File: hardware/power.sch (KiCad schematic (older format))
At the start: 34 parts, among them U1 TPS54526_PWP, U2 LT1761_1, U3 MIC2774N

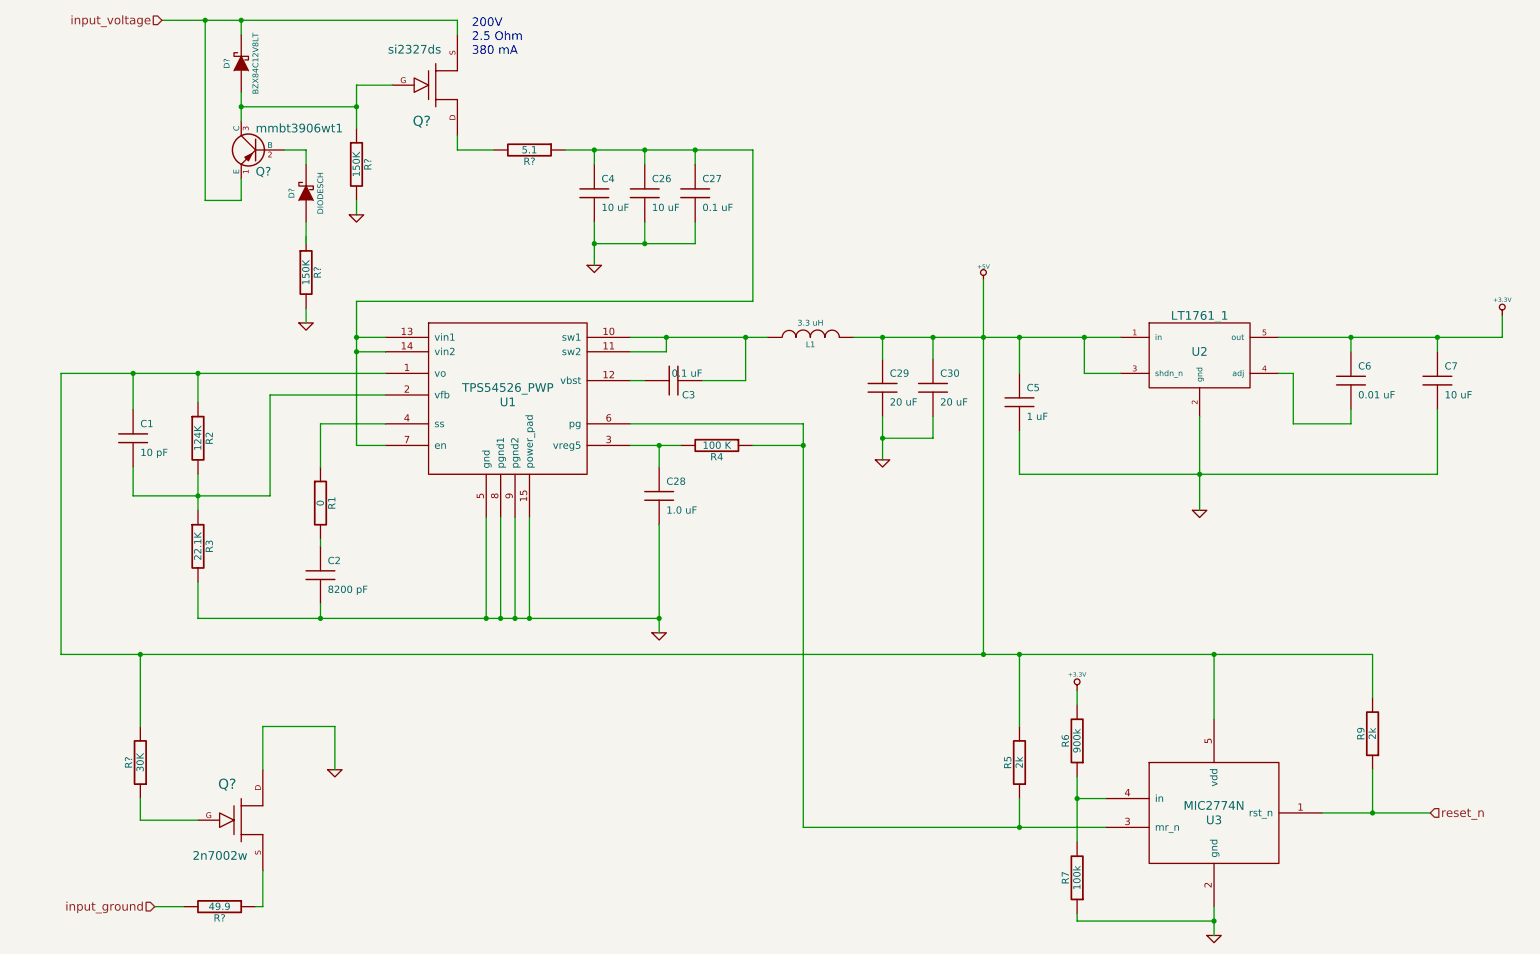
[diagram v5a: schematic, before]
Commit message: added RCT and accellerometer, added new sheet
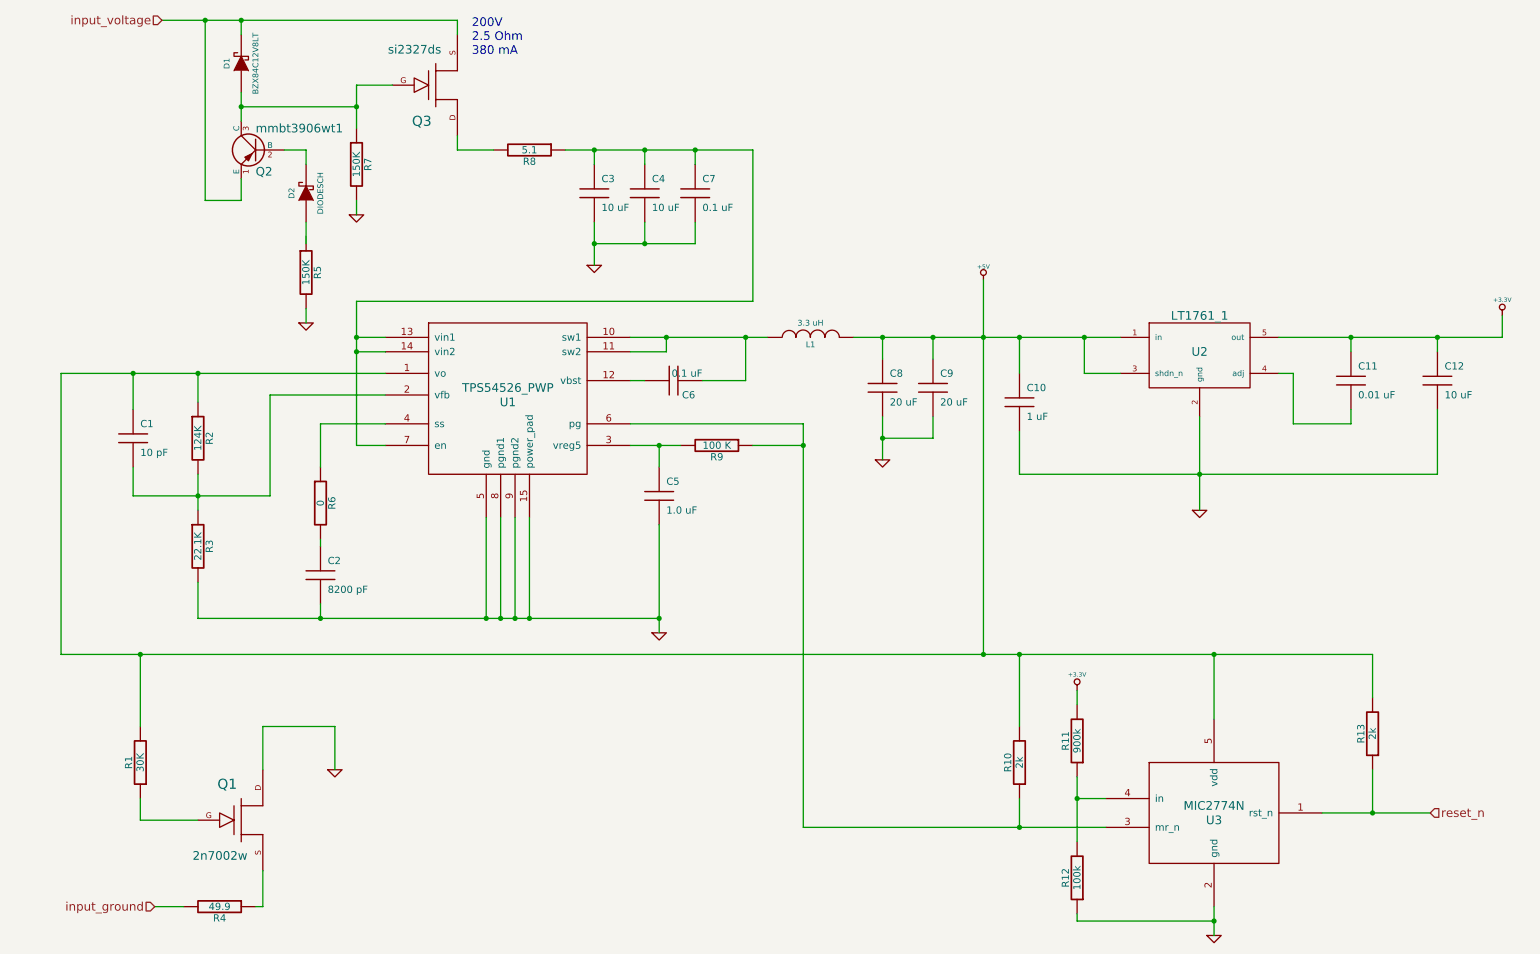
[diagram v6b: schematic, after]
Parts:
- gave numbers to parts that had none: 10
- renumbered C5 to C10, C6 to C11, C7 to C12, C4 to C3, C26 to C4, C28 to C5, C3 to C6, C27 to C7, C29 to C8, C30 to C9, R5 to R10, R6 to R11, R7 to R12, R9 to R13, R1 to R6, R4 to R9
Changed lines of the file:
@@
-EESchema Schematic File Version 2  date Thu 07 Nov 2013 07:55:20 AM EST
+EESchema Schematic File Version 2  date Tue 12 Nov 2013 10:09:33 PM EST
 LIBS:power
 LIBS:device
@@
 $Descr A4 11700 8267
 encoding utf-8
-Sheet 2 5
+Sheet 2 6
 Title ""
-Date "7 nov 2013"
+Date "13 nov 2013"
 Rev ""
 Comp ""
@@
 Connection ~ 4550 1600
 $Comp
-L R R?
+L R R8
 U 1 1 527B8B5E
 P 4100 1600
-F 0 "R?" V 4180 1600 50  0000 C CNN
+F 0 "R8" V 4180 1600 50  0000 C CNN
 F 1 "5.1" V 4100 1600 50  0000 C CNN
 	1    4100 1600
@@
 200V \n2.5 Ohm \n380 mA
 $Comp
-L FET_N Q?
+L FET_N Q3
 U 1 1 527B8896
 P 3450 1150
-F 0 "Q?" H 3353 1400 70  0000 C CNN
+F 0 "Q3" H 3353 1400 70  0000 C CNN
 F 1 "si2327ds" H 3303 903 60  0000 C CNN
 	1    3450 1150
@@
 $EndComp
 $Comp
-L R R?
+L R R7
 U 1 1 527B886A
 P 2900 1700
-F 0 "R?" V 2980 1700 50  0000 C CNN
+F 0 "R7" V 2980 1700 50  0000 C CNN
 F 1 "150K" V 2900 1700 50  0000 C CNN
 	1    2900 1700
@@
 $EndComp
 $Comp
-L GND #PWR?
+L GND #PWR01
 U 1 1 527B8869
 P 2900 2050
-F 0 "#PWR?" H 2900 2050 30  0001 C CNN
+F 0 "#PWR01" H 2900 2050 30  0001 C CNN
 F 1 "GND" H 2900 1980 30  0001 C CNN
 	1    2900 2050
@@
 $EndComp
 $Comp
-L DIODESCH D?
+L DIODESCH D1
 U 1 1 527B8850
 P 2100 1000
-F 0 "D?" H 2100 1100 40  0000 C CNN
+F 0 "D1" H 2100 1100 40  0000 C CNN
 F 1 "BZX84C12V8LT" H 2100 900 40  0000 C CNN
 	1    2100 1000
@@
 $EndComp
 $Comp
-L GND #PWR?
+L GND #PWR02
 U 1 1 527B883D
 P 2550 2800
-F 0 "#PWR?" H 2550 2800 30  0001 C CNN
+F 0 "#PWR02" H 2550 2800 30  0001 C CNN
 F 1 "GND" H 2550 2730 30  0001 C CNN
 	1    2550 2800
@@
 $EndComp
 $Comp
-L R R?
+L R R5
 U 1 1 527B882C
 P 2550 2450
-F 0 "R?" V 2630 2450 50  0000 C CNN
+F 0 "R5" V 2630 2450 50  0000 C CNN
 F 1 "150K" V 2550 2450 50  0000 C CNN
 	1    2550 2450
@@
 $EndComp
 $Comp
-L R R?
+L R R4
 U 1 1 527B85F0
 P 1950 6850
-F 0 "R?" V 2030 6850 50  0000 C CNN
+F 0 "R4" V 2030 6850 50  0000 C CNN
 F 1 "49.9" V 1950 6850 50  0000 C CNN
 	1    1950 6850
@@
 $EndComp
 $Comp
-L GND #PWR?
+L GND #PWR03
 U 1 1 527B85B8
 P 2750 5900
-F 0 "#PWR?" H 2750 5900 30  0001 C CNN
+F 0 "#PWR03" H 2750 5900 30  0001 C CNN
 F 1 "GND" H 2750 5830 30  0001 C CNN
 	1    2750 5900
@@
 $EndComp
 $Comp
-L R R?
+L R R1
 U 1 1 527B8568
 P 1400 5850
-F 0 "R?" V 1480 5850 50  0000 C CNN
+F 0 "R1" V 1480 5850 50  0000 C CNN
 F 1 "30K" V 1400 5850 50  0000 C CNN
 	1    1400 5850
@@
 $EndComp
 $Comp
-L FET_N Q?
+L FET_N Q1
 U 1 1 527B8523
 P 2100 6250
-F 0 "Q?" H 2003 6500 70  0000 C CNN
+F 0 "Q1" H 2003 6500 70  0000 C CNN
 F 1 "2n7002w" H 1953 6003 60  0000 C CNN
 	1    2100 6250
@@
 $EndComp
 $Comp
-L PNP Q?
+L PNP Q2
 U 1 1 527B8379
 P 2200 1600
-F 0 "Q?" H 2200 1450 60  0000 R CNN
+F 0 "Q2" H 2200 1450 60  0000 R CNN
 F 1 "mmbt3906wt1" H 2200 1750 60  0000 R CNN
 	1    2200 1600
@@
 $EndComp
 $Comp
-L DIODESCH D?
+L DIODESCH D2
 U 1 1 527B82DF
 P 2550 1900
-F 0 "D?" H 2550 2000 40  0000 C CNN
+F 0 "D2" H 2550 2000 40  0000 C CNN
 F 1 "DIODESCH" H 2550 1800 40  0000 C CNN
 	1    2550 1900
@@
 $EndComp
 $Comp
-L C C28
+L C C5
 U 1 1 5278578C
 P 5000 4000
-F 0 "C28" H 5050 4100 50  0000 L CNN
+F 0 "C5" H 5050 4100 50  0000 L CNN
 F 1 "1.0 uF" H 5050 3900 50  0000 L CNN
 	1    5000 4000
@@
 $EndComp
 $Comp
-L R R4
+L R R9
 U 1 1 52785766
 P 5400 3650
-F 0 "R4" V 5480 3650 50  0000 C CNN
+F 0 "R9" V 5480 3650 50  0000 C CNN
 F 1 "100 K" V 5400 3650 50  0000 C CNN
 	1    5400 3650
@@
 $EndComp
 $Comp
-L C C29
+L C C8
 U 1 1 527852FE
 P 6550 3250
-F 0 "C29" H 6600 3350 50  0000 L CNN
+F 0 "C8" H 6600 3350 50  0000 L CNN
 F 1 "20 uF" H 6600 3150 50  0000 L CNN
 	1    6550 3250
@@
 $EndComp
 $Comp
-L C C30
+L C C9
 U 1 1 527852FD
 P 6900 3250
-F 0 "C30" H 6950 3350 50  0000 L CNN
+F 0 "C9" H 6950 3350 50  0000 L CNN
 F 1 "20 uF" H 6950 3150 50  0000 L CNN
 	1    6900 3250
@@
 $EndComp
 $Comp
-L GND #PWR01
+L GND #PWR04
 U 1 1 527852FC
 P 6550 3750
-F 0 "#PWR01" H 6550 3750 30  0001 C CNN
+F 0 "#PWR04" H 6550 3750 30  0001 C CNN
 F 1 "GND" H 6550 3680 30  0001 C CNN
 	1    6550 3750
@@
 $EndComp
 $Comp
-L C C3
+L C C6
 U 1 1 526D9BDC
 P 5100 3200
-F 0 "C3" V 5000 3050 50  0000 L CNN
+F 0 "C6" V 5000 3050 50  0000 L CNN
 F 1 "0.1 uF" V 5150 3000 50  0000 L CNN
 	1    5100 3200
@@
 $EndComp
 $Comp
-L GND #PWR02
+L GND #PWR05
 U 1 1 526D9921
 P 5000 4950
-F 0 "#PWR02" H 5000 4950 30  0001 C CNN
+F 0 "#PWR05" H 5000 4950 30  0001 C CNN
 F 1 "GND" H 5000 4880 30  0001 C CNN
 	1    5000 4950
@@
 $EndComp
 $Comp
-L GND #PWR03
+L GND #PWR06
 U 1 1 52784FA3
 P 4550 2400
-F 0 "#PWR03" H 4550 2400 30  0001 C CNN
+F 0 "#PWR06" H 4550 2400 30  0001 C CNN
 F 1 "GND" H 4550 2330 30  0001 C CNN
 	1    4550 2400
@@
 $EndComp
 $Comp
-L C C27
+L C C7
 U 1 1 52784F6E
 P 5250 1900
-F 0 "C27" H 5300 2000 50  0000 L CNN
+F 0 "C7" H 5300 2000 50  0000 L CNN
 F 1 "0.1 uF" H 5300 1800 50  0000 L CNN
 	1    5250 1900
@@
 $EndComp
 $Comp
-L C C26
+L C C4
 U 1 1 52784F63
 P 4900 1900
-F 0 "C26" H 4950 2000 50  0000 L CNN
+F 0 "C4" H 4950 2000 50  0000 L CNN
 F 1 "10 uF" H 4950 1800 50  0000 L CNN
 	1    4900 1900
@@
 $EndComp
 $Comp
-L C C4
+L C C3
 U 1 1 52784F2D
 P 4550 1900
-F 0 "C4" H 4600 2000 50  0000 L CNN
+F 0 "C3" H 4600 2000 50  0000 L CNN
 F 1 "10 uF" H 4600 1800 50  0000 L CNN
 	1    4550 1900
@@
 $EndComp
 $Comp
-L R R1
+L R R6
 U 1 1 526E4AF9
 P 2650 4050
-F 0 "R1" V 2730 4050 50  0000 C CNN
+F 0 "R6" V 2730 4050 50  0000 C CNN
 F 1 "0" V 2650 4050 50  0000 C CNN
 	1    2650 4050
@@
 $EndComp
 $Comp
-L +3.3V #PWR04
+L +3.3V #PWR07
 U 1 1 526E4845
 P 7900 5350
-F 0 "#PWR04" H 7900 5310 30  0001 C CNN
+F 0 "#PWR07" H 7900 5310 30  0001 C CNN
 F 1 "+3.3V" H 7900 5460 30  0000 C CNN
 	1    7900 5350
@@
 $EndComp
 $Comp
-L R R7
+L R R12
 U 1 1 526E4836
 P 7900 6650
-F 0 "R7" V 7980 6650 50  0000 C CNN
+F 0 "R12" V 7980 6650 50  0000 C CNN
 F 1 "100k" V 7900 6650 50  0000 C CNN
 	1    7900 6650
@@
 $EndComp
 $Comp
-L R R6
+L R R11
 U 1 1 526E482D
 P 7900 5700
-F 0 "R6" V 7980 5700 50  0000 C CNN
+F 0 "R11" V 7980 5700 50  0000 C CNN
 F 1 "900k" V 7900 5700 50  0000 C CNN
 	1    7900 5700
@@
 $EndComp
 $Comp
-L R R5
+L R R10
 U 1 1 526E4807
 P 7500 5850
-F 0 "R5" V 7580 5850 50  0000 C CNN
+F 0 "R10" V 7580 5850 50  0000 C CNN
 F 1 "2k" V 7500 5850 50  0000 C CNN
 	1    7500 5850
@@
 $EndComp
 $Comp
-L GND #PWR05
+L GND #PWR08
 U 1 1 526E46E4
 P 8850 7050
-F 0 "#PWR05" H 8850 7050 30  0001 C CNN
+F 0 "#PWR08" H 8850 7050 30  0001 C CNN
 F 1 "GND" H 8850 6980 30  0001 C CNN
 	1    8850 7050
@@
 reset_n
 $Comp
-L C C6
+L C C11
 U 1 1 526DB018
 P 9800 3200
-F 0 "C6" H 9850 3300 50  0000 L CNN
+F 0 "C11" H 9850 3300 50  0000 L CNN
 F 1 "0.01 uF" H 9850 3100 50  0000 L CNN
 	1    9800 3200
@@
 $EndComp
 $Comp
-L +3.3V #PWR07
+L +3.3V #PWR09
 U 1 1 526DAF40
 P 10850 2750
-F 0 "#PWR07" H 10850 2710 30  0001 C CNN
+F 0 "#PWR09" H 10850 2710 30  0001 C CNN
 F 1 "+3.3V" H 10850 2860 30  0000 C CNN
 	1    10850 2750
@@
 $EndComp
 $Comp
-L C C7
+L C C12
 U 1 1 526DAED8
 P 10400 3200
-F 0 "C7" H 10450 3300 50  0000 L CNN
+F 0 "C12" H 10450 3300 50  0000 L CNN
 F 1 "10 uF" H 10450 3100 50  0000 L CNN
 	1    10400 3200
@@
 $EndComp
 $Comp
-L GND #PWR08
+L GND #PWR010
 U 1 1 526DAE70
 P 8750 4100
-F 0 "#PWR08" H 8750 4100 30  0001 C CNN
+F 0 "#PWR010" H 8750 4100 30  0001 C CNN
 F 1 "GND" H 8750 4030 30  0001 C CNN
 	1    8750 4100
@@
 $EndComp
 $Comp
-L C C5
+L C C10
 U 1 1 526DAE33
 P 7500 3350
-F 0 "C5" H 7550 3450 50  0000 L CNN
+F 0 "C10" H 7550 3450 50  0000 L CNN
 F 1 "1 uF" H 7550 3250 50  0000 L CNN
 	1    7500 3350
@@
 $EndComp
 $Comp
-L R R9
+L R R13
 U 1 1 526D9B03
 P 9950 5650
-F 0 "R9" V 10030 5650 50  0000 C CNN
+F 0 "R13" V 10030 5650 50  0000 C CNN
 F 1 "2k" V 9950 5650 50  0000 C CNN
 	1    9950 5650
@@
 $EndComp
 $Comp
-L +5V #PWR09
+L +5V #PWR011
 U 1 1 526D9802
 P 7250 2500
-F 0 "#PWR09" H 7250 2590 20  0001 C CNN
+F 0 "#PWR011" H 7250 2590 20  0001 C CNN
 F 1 "+5V" H 7250 2590 30  0000 C CNN
 	1    7250 2500
